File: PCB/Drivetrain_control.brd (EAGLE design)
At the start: 92.7 x 107.6 mm, 27 parts, among them IC1 LM358N, J1 SSW-110-02-G-S, J2 SSW-110-02-G-S, J3 SSW-110-02-G-S, J4 SSW-110-02-G-S, J5 SSW-110-02-G-S, J6 SSW-110-02-G-S, J7 SSW-110-02-G-S, J8 SSW-110-02-G-S, Q1 IRFI540NPBF, Q2 IRFI540NPBF, Q3 IRFI540NPBF, Q4 IRFI540NPBF, Q5 IRFI540NPBF

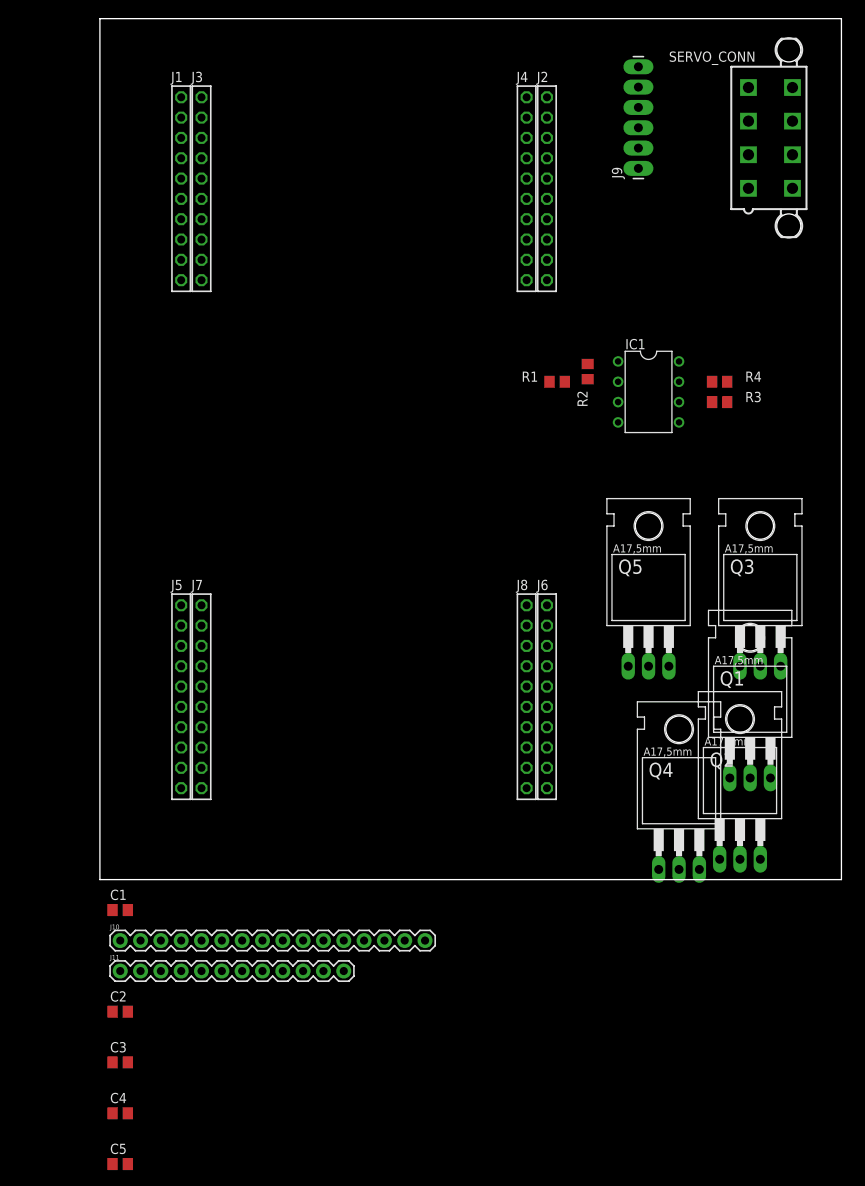
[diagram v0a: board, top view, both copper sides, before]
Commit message: Added outputs to servo connector
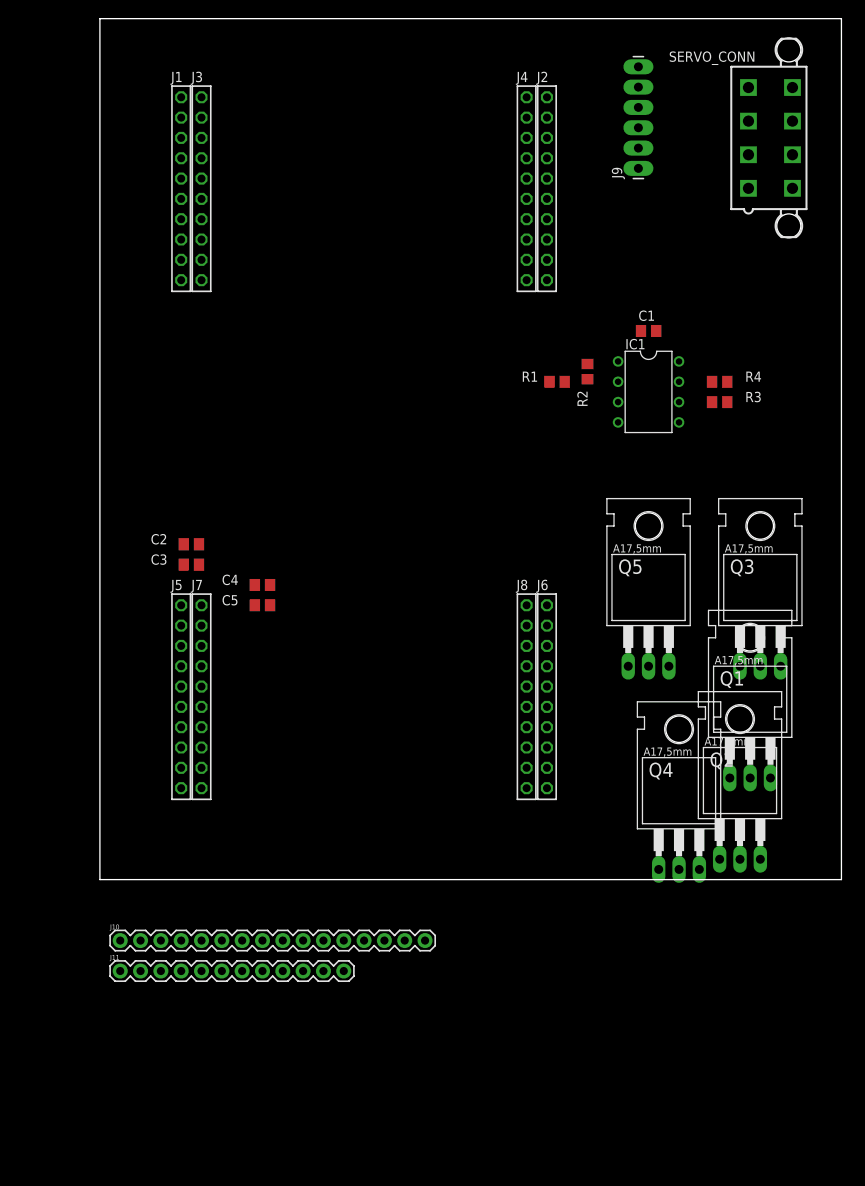
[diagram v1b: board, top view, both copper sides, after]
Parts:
- moved C1 98.0 mm to (68.6, 68.6)
- moved C5 72.1 mm to (20.3, 34.3)
- moved C4 68.4 mm to (20.3, 36.8)
- moved C3 62.9 mm to (11.4, 39.4)
- moved C2 59.1 mm to (11.4, 41.9)
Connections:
- removed net N$4: IC1.1, R2.1
- new net EN+: SERVO_CONN.4
- new net HLFB+: SERVO_CONN.1
- new net INPUT_A+: SERVO_CONN.3
- new net INPUT_B+: IC1.1, R2.1, SERVO_CONN.2
- net GND: now also SERVO_CONN.5, SERVO_CONN.6, SERVO_CONN.7, SERVO_CONN.8

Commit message: Preliminary Layout
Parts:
- removed J10: (no value), SparkFun-Connectors:1X16
- removed J11: (no value), SparkFun-Connectors:1X12
- removed Q2, Q3, Q4, Q5: IRFI540NPBF, transistor-power:TO220BH
- added BRAKE_CONN: 1X2-3.5MM, adafruit:1X2-3.5MM
- added DCDC_CONN, JETSON_CONN: 22-23-2021, con-molex:22-23-2021
- added MC_CONN: 22-23-2031, con-molex:22-23-2031
- added MS1: FEATHERWING_NODIM, adafruit:FEATHERWING_DIM
- added Q10, Q6, Q7, Q8, Q9: 100V/17A, SparkFun-DiscreteSemi:TO220V
- added R5: (no value), resistor:R0805
- Q1: value IRFI540NPBF -> 220mA/50V/3.5Ω; device transistor-power:TO220BH -> SparkFun-DiscreteSemi:SOT23-3
- moved Q1 85.2 mm to (34.3, 90.2)
- moved C1 66.6 mm to (19.1, 24.1)
- moved IC1 66.6 mm to (19.1, 16.5)
- moved R3 66.6 mm to (27.9, 15.2)
- moved R4 66.6 mm to (27.9, 17.8)
- moved R1 35.3 mm to (39.4, 92.7)
- moved R2 32.4 mm to (39.4, 87.6), turned to 0 degrees
- moved J2 5.08 mm to (50.8, 86.4)
- moved J4 5.08 mm to (48.3, 86.4)
- moved J6 5.08 mm to (50.8, 22.9)
- moved J8 5.08 mm to (48.3, 22.9)
- moved C2 5.08 mm to (6.35, 41.9)
- moved C3 5.08 mm to (6.35, 39.4)
- moved C4 5.08 mm to (15.2, 36.8)
- moved C5 5.08 mm to (15.2, 34.3)
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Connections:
- removed net EN_SERVO: Q1.D
- removed net N$3: IC1.2, R1.2, R2.2
- removed net N$5: Q1.G
- removed net N$6: Q4.G
- removed net N$7: Q2.G
- removed net N$8: Q5.G
- removed net N$9: Q3.G
- new net PWM_12V: Q1.3, R2.1
- new net TI_PWM: Q1.2, R1.1
- net +12V: now also BRAKE_CONN.1, DCDC_CONN.1, R2.2, R5.2
- net +3V3: now also JETSON_CONN.1, MS1.2, Q1.1, R1.2
- net BRAKE_SOLENOID: now also BRAKE_CONN.2, Q10.2; no longer Q5.D
- net EN+: now also Q6.2, R5.1
- net FS1_MC: now also MC_CONN.1, Q9.2; no longer Q2.D
- net FWD_MC: now also MC_CONN.2, Q8.2; no longer Q3.D
- net GND: now also DCDC_CONN.2, JETSON_CONN.2, MS1.4, Q10.3, Q6.3, Q7.3, Q8.3, Q9.3; no longer Q1.S, Q2.S, Q3.S, Q4.S, Q5.S, R1.1
- net INPUT_B+: no longer IC1.1, R2.1
- net REV_MC: now also MC_CONN.3, Q7.2; no longer Q4.D
- net STEERING_PWM: no longer IC1.3
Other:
- board size 92.7 x 107.6 mm -> 92.7 x 112.7 mm

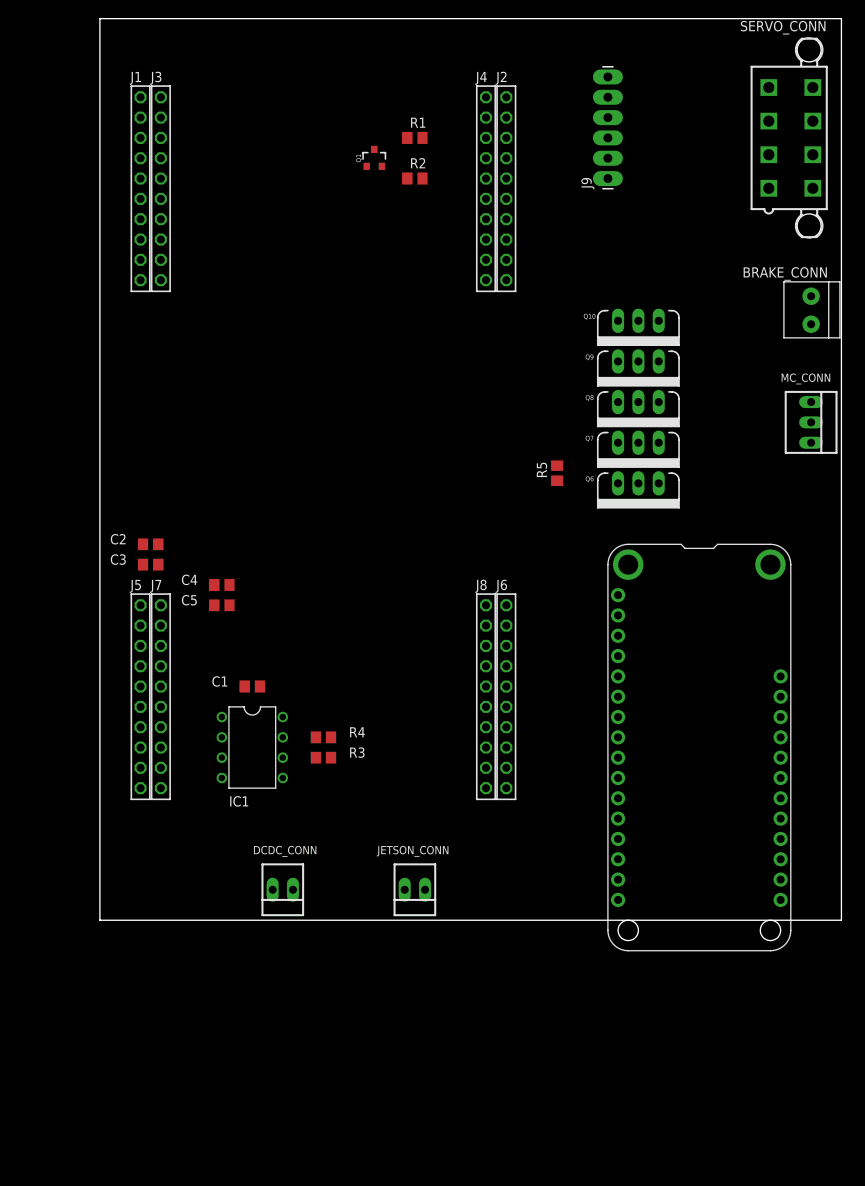
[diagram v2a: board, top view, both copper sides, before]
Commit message: Feather pins added
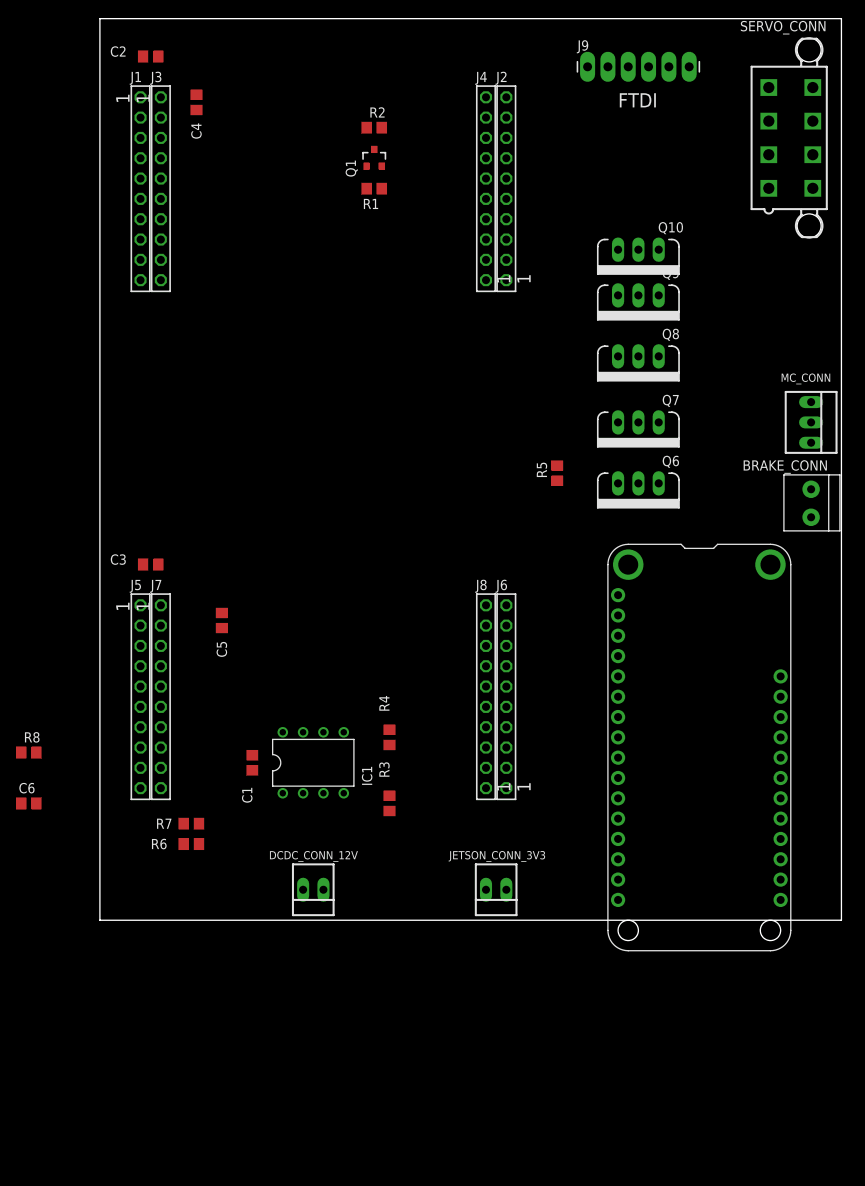
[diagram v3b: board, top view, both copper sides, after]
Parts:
- removed DCDC_CONN, JETSON_CONN: 22-23-2021, con-molex:22-23-2021
- added C6: 0.1uF, eagle-ltspice:C0805
- added DCDC_CONN_12V, JETSON_CONN_3V3: 22-23-2021, con-molex:22-23-2021
- added R6, R7: 4.7k, resistor:R0805
- added R8: DNP, resistor:R0805
- R1, R2: value (none) -> 10k
- moved C2 61.0 mm to (6.35, 102.9)
- moved C4 60.4 mm to (12.1, 97.2), turned to 270 degrees
- moved BRAKE_CONN 24.1 mm to (88.9, 47.0)
- moved J9 14.2 mm to (61.0, 101.6), turned to 0 degrees
- moved R3 10.0 mm to (36.2, 9.53), turned to 90 degrees
- moved C1 9.52 mm to (19.1, 14.6), turned to 90 degrees
- moved Q10 8.89 mm to (67.3, 78.7)
- moved Q9 8.26 mm to (67.3, 73.0)
- moved R4 8.25 mm to (36.2, 17.8), turned to 90 degrees
- moved R2 8.13 mm to (34.3, 94.0)
- moved R1 8.13 mm to (34.3, 86.4), turned to 180 degrees
- moved IC1 7.85 mm to (26.7, 14.6), turned to 0 degrees
- moved Q8 5.72 mm to (67.3, 65.4)
- moved Q7 2.54 mm to (67.3, 57.1)
- moved C5 1.91 mm to (15.2, 32.4), turned to 270 degrees
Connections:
- new net KILL_SIGNAL: MS1.19, Q10.1
- new net N$3: MS1.27, R8.2
- net +12V: now also DCDC_CONN_12V.1; no longer DCDC_CONN.1
- net +3V3: now also JETSON_CONN_3V3.1, R6.2, R7.2; no longer JETSON_CONN.1, MS1.2
- net +5V: now also C6.1, MS1.26
- net GND: now also C6.2, DCDC_CONN_12V.2, JETSON_CONN_3V3.2, R8.1; no longer DCDC_CONN.2, JETSON_CONN.2
- net GPIO40/I2CSDAB/J5: now also MS1.17, R6.1
- net GPIO41/I2CSCLB/J5: now also MS1.18, R7.1
- net GPIO95: now also MS1.1
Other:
- board text added: "FTDI"

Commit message: Finished Schematic and Routing, Version 1.0
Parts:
- removed J9: (no value), SparkFun-Connectors:1X06_LONGPADS
- removed JETSON_CONN_3V3: 22-23-2021, con-molex:22-23-2021
- added D1: 1N4004, diode:DO41-10
- added ENCODER_CONN, JETSON_CONN_PWR: 22-23-2031, con-molex:22-23-2031
- added FTDI: (no value), SparkFun-Connectors:1X06_LONGPADS
- added Q2: 100V/17A, SparkFun-DiscreteSemi:TO220V
- added R10, R11, R12, R13, R14, R15, R16, R17, R18, R9: (no value), resistor:R0805
- MC_CONN: value 22-23-2031 -> 22-23-2041; device con-molex:22-23-2031 -> con-molex:22-23-2041
- moved DCDC_CONN_12V 116.2 mm to (75.6, 104.1), turned to 0 degrees
- moved R8 99.9 mm to (90.8, 21.6), turned to 90 degrees
- moved C6 96.6 mm to (87.0, 21.6), turned to 270 degrees
- moved C1 49.4 mm to (26.0, 63.5), turned to 180 degrees
- moved R3 42.6 mm to (33.7, 52.0)
- moved IC1 41.9 mm to (26.0, 56.5), turned to 270 degrees
- moved R4 38.5 mm to (33.7, 56.2), turned to 270 degrees
- moved Q6 34.9 mm to (67.9, 84.5)
- moved Q10 29.2 mm to (67.9, 49.5)
- moved R5 28.9 mm to (57.1, 79.7), turned to 270 degrees
- moved Q1 10.3 mm to (36.2, 100.3)
- moved R1 9.09 mm to (36.2, 95.2)
- moved R2 5.99 mm to (31.1, 99.1), turned to 270 degrees
- moved MC_CONN 5.72 mm to (88.9, 62.9)
- moved C5 5.24 mm to (10.2, 33.7)
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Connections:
- net GPIO40/I2CSDAB/J5 renamed I2CSDAB
- net GPIO41/I2CSCLB/J5 renamed I2CSCLB
- net GPIO95 renamed FEATHER_RESET
- removed net GPIO10/PWMOUT6A: J8.6
- removed net GPIO11/PWMOUT6B: J8.5
- removed net GPIO14/OPXBAR3: J8.4
- removed net GPIO16/OPXBAR7: J4.3
- removed net GPIO18: J1.4, J9.4
- removed net GPIO19: J1.3, J9.5
- removed net GPIO24/OPXBAR1: J4.4
- removed net GPIO6/PWMOUT4A: J8.10
- removed net GPIO7/PWMOUT4B: J8.9
- removed net GPIO8/PWMOUT5A: J8.8
- removed net GPIO9/PWMOUT5B: J8.7
- removed net PWM_12V: Q1.3, R2.1
- new net EN+_CTL: J4.4, Q6.1
- new net ENCODER_U: ENCODER_CONN.1, R12.2
- new net ENCODER_V: ENCODER_CONN.2, R11.2
- new net ENCODER_W: ENCODER_CONN.3, R10.2
- new net FS1_CTL: J8.10, Q9.1
- new net FWD_CTL: J8.9, Q8.1
- new net INPUT_A+_CTL: J4.3, Q2.1
- new net MC_HLFB+: J8.4, R16.1, R17.2
- new net MC_U: J8.7, R12.1, R15.2
- new net MC_V: J8.6, R11.1, R14.2
- new net MC_W: J8.5, R10.1, R13.2
- new net REV_CTL: J8.8, Q7.1
- new net SCIB_RX: FTDI.5, J1.3
- new net SCIB_TX: FTDI.4, J1.4
- new net THROTTLE_MC: IC1.7, MC_CONN.4, R4.1
- net +12V: now also R18.2, R9.2
- net +3V3: now also FTDI.3, JETSON_CONN_PWR.2; no longer J9.3, JETSON_CONN_3V3.1
- net +5V: now also JETSON_CONN_PWR.1
- net BRAKE_SOLENOID: now also D1.A
- net GND: now also FTDI.1, JETSON_CONN_PWR.3, Q2.3, R13.1, R14.1, R15.1, R17.1; no longer J9.1, JETSON_CONN_3V3.2
- net HLFB+: now also R16.2
- net INPUT_A+: now also Q2.2, R18.1
- net INPUT_B+: now also Q1.3, R2.1
- net N$2: now also D1.C, R9.1; no longer IC1.7, R4.1
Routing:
- net +5V: track 0.00 -> 192.9 mm, vias 0 -> 2
- net MC_HLFB+: track 0.00 -> 105.3 mm, vias 0 -> 2
- net I2CSCLB: track 0.00 -> 93.5 mm, vias 0 -> 3
- net MC_W: track 0.00 -> 93.2 mm, vias 0 -> 2
- net I2CSDAB: track 0.00 -> 92.5 mm, vias 0 -> 1
- net MC_V: track 0.00 -> 91.5 mm, vias 0 -> 2
- net MC_U: track 0.00 -> 90.7 mm, vias 0 -> 2
- net SCIB_TX: track 0.00 -> 79.3 mm, vias 0 -> 3
- net SCIB_RX: track 0.00 -> 76.7 mm, vias 0 -> 3
- net THROTTLE_DAC: track 0.00 -> 64.3 mm, vias 0 -> 2
- net INPUT_B+: track 0.00 -> 63.1 mm, vias 0 -> 2
- net FEATHER_RESET: track 0.00 -> 62.5 mm, vias 0 -> 2
- net THROTTLE_MC: track 0.00 -> 60.1 mm
- net FS1_CTL: track 0.00 -> 59.6 mm, vias 0 -> 3
- net KILL_SIGNAL: track 0.00 -> 55.9 mm, vias 0 -> 1
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- added copper zone on layer 16, net +12V
- added copper zone on layer 1, net +3V3
- added copper zone on layer 16, net +3V3
- added copper zone on layer 1, net GND
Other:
- board size 92.7 x 112.7 mm -> 94 x 109.9 mm
- board text removed: "FTDI"

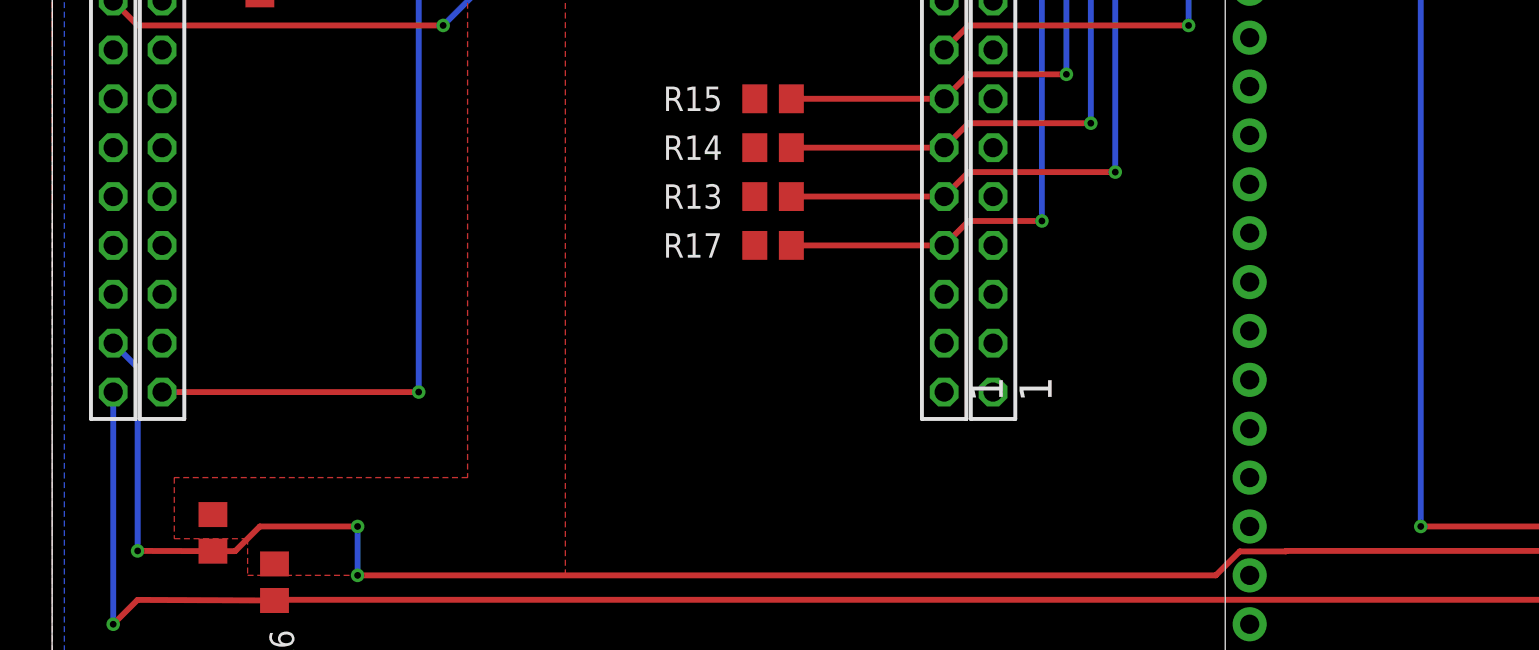
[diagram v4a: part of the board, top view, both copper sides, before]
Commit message: Added Kill Signal route to GPIO pin of TI
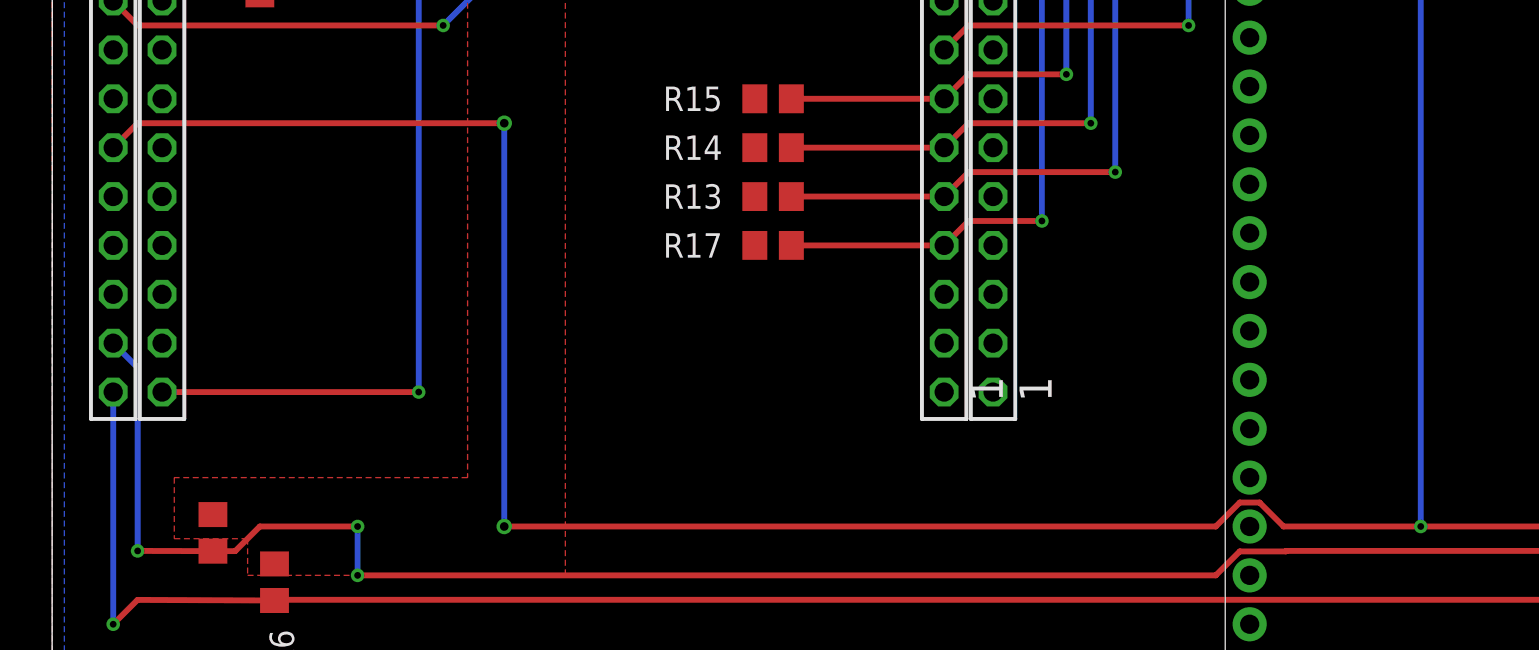
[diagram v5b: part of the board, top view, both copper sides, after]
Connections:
- removed net GPIO97: J5.5
- net KILL_SIGNAL: now also J5.5
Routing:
- net KILL_SIGNAL: track 55.9 -> 146.3 mm, vias 1 -> 3
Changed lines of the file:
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@@
 <contactref element="J5" pad="4"/>
-</signal>
-<signal name="GPIO97">
-<contactref element="J5" pad="5"/>
 </signal>
 <signal name="GPIO94">
@@
 <via x="70.485" y="5.08" extent="1-16" drill="0.35"/>
 <wire x1="70.485" y1="5.08" x2="81.915" y2="5.08" width="0.3048" layer="1"/>
+<contactref element="J5" pad="5"/>
+<wire x1="62.11053125" y1="6.3246" x2="61.07946875" y2="6.3246" width="0.3048" layer="1"/>
+<wire x1="70.485" y1="5.08" x2="63.35513125" y2="5.08" width="0.3048" layer="1"/>
+<wire x1="59.83486875" y1="5.08" x2="22.86" y2="5.08" width="0.3048" layer="1"/>
+<wire x1="63.35513125" y1="5.08" x2="62.11053125" y2="6.3246" width="0.3048" layer="1"/>
+<wire x1="61.07946875" y1="6.3246" x2="59.83486875" y2="5.08" width="0.3048" layer="1"/>
+<via x="22.86" y="5.08" extent="1-16" drill="0.45"/>
+<wire x1="22.86" y1="5.08" x2="22.86" y2="26.035" width="0.3048" layer="16"/>
+<via x="22.86" y="26.035" extent="1-16" drill="0.45"/>
+<wire x1="22.86" y1="26.035" x2="3.81" y2="26.035" width="0.3048" layer="1"/>
+<wire x1="3.81" y1="26.035" x2="2.54" y2="24.765" width="0.3048" layer="1"/>
 </signal>
 <signal name="N$3">
